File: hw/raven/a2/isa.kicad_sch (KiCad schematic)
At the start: 24 parts, among them U108 ATF22V10C-10PU

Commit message: Raven.A2 wip
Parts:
- gave numbers to parts that had none: 5
- renumbered C9 to C501, U108 to U501

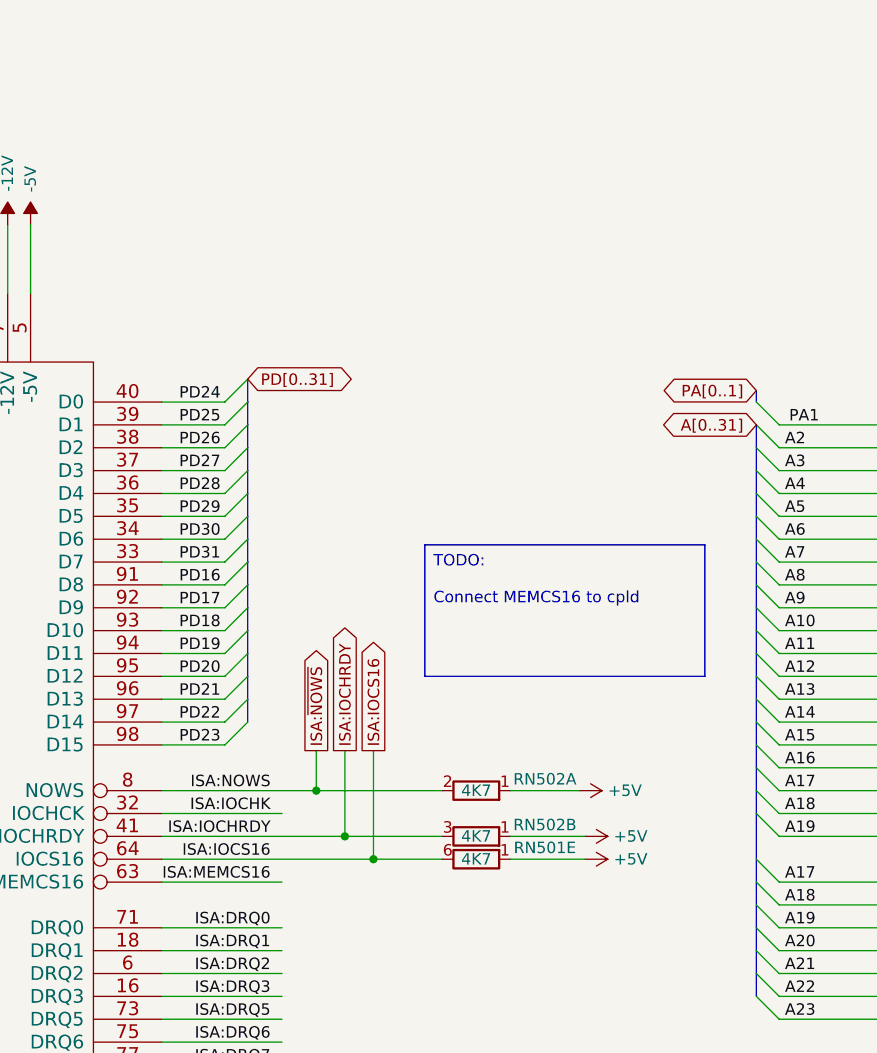
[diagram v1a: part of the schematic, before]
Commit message: ISA:MEMCS16 for 8bit support
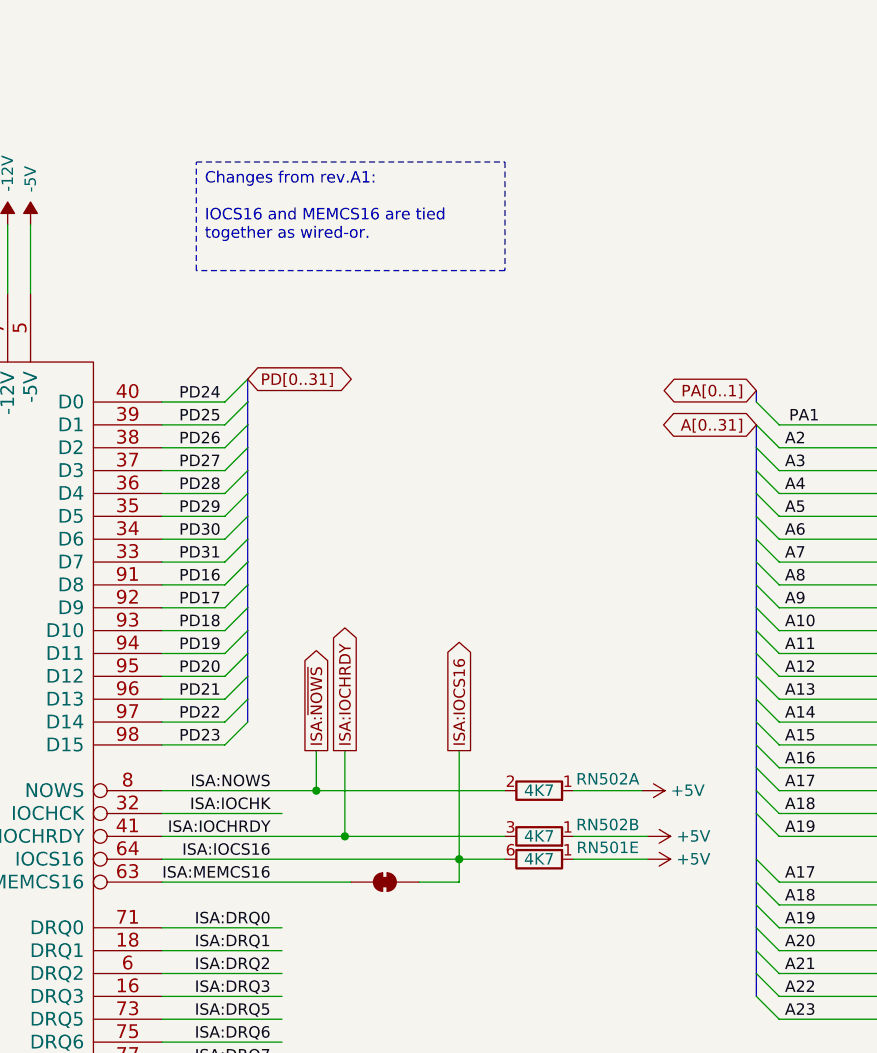
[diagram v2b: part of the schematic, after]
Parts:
- added JP501: SolderJumper_2_Bridged, Jumper:SolderJumper-2_P1.3mm_Bridged_RoundedPad1.0x1.5mm, symbol Jumper:SolderJumper_2_Bridged
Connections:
- net ISA:IOCS16: now also JP501.2 (B)
- net ISA:MEMCS16: now also JP501.1 (A)
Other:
- moved on the sheet: RN501E, RN502A, RN502B

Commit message: a2
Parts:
- JP501: footprint Jumper:SolderJumper-2_P1.3mm_Bridged_RoundedPad1.0x1.5mm -> Jumper:SolderJumper-2_P1.3mm_Open_RoundedPad1.0x1.5mm
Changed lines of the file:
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@@
 			)
 		)
-		(property "Footprint" "Jumper:SolderJumper-2_P1.3mm_Bridged_RoundedPad1.0x1.5mm"
+		(property "Footprint" "Jumper:SolderJumper-2_P1.3mm_Open_RoundedPad1.0x1.5mm"
 			(at 168.275 272.415 0)
 			(effects

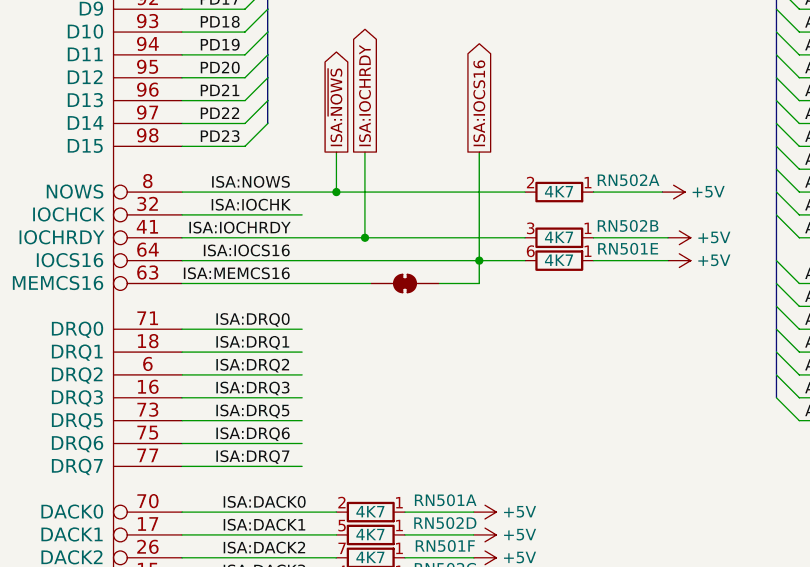
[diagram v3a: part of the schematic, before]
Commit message: A2: support 32MB simms
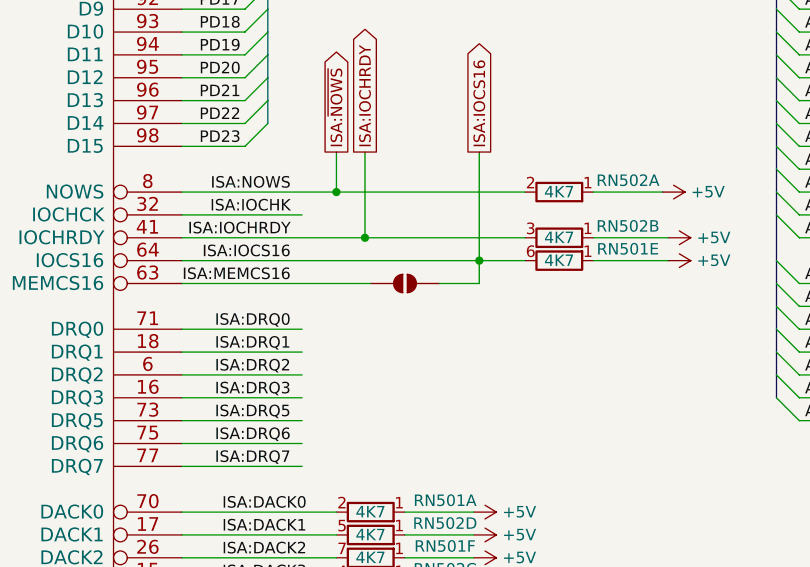
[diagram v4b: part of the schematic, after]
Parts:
- JP501: symbol Jumper:SolderJumper_2_Bridged -> Jumper:SolderJumper_2_Open
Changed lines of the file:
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@@
 	)
 	(symbol
-		(lib_id "Jumper:SolderJumper_2_Bridged")
+		(lib_id "Jumper:SolderJumper_2_Open")
 		(at 168.275 272.415 0)
 		(unit 1)
@@
 			)
 		)
-		(property "Description" "Solder Jumper, 2-pole, closed/bridged"
+		(property "Description" "Solder Jumper, 2-pole, open"
 			(at 168.275 272.415 0)
 			(effects
